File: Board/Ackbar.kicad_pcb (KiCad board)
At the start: 2 copper layers, 101.6 x 50.8 mm, 14 parts, among them J1 TOF, J2 GNSS, J3 HALL, J4 MOTOR, J5 PWR_IN, J6 EPD, U1 ESP32-S3 Pico, U2 VREG, U3 TMC2209, U4 SN74LVC1G04DCKR

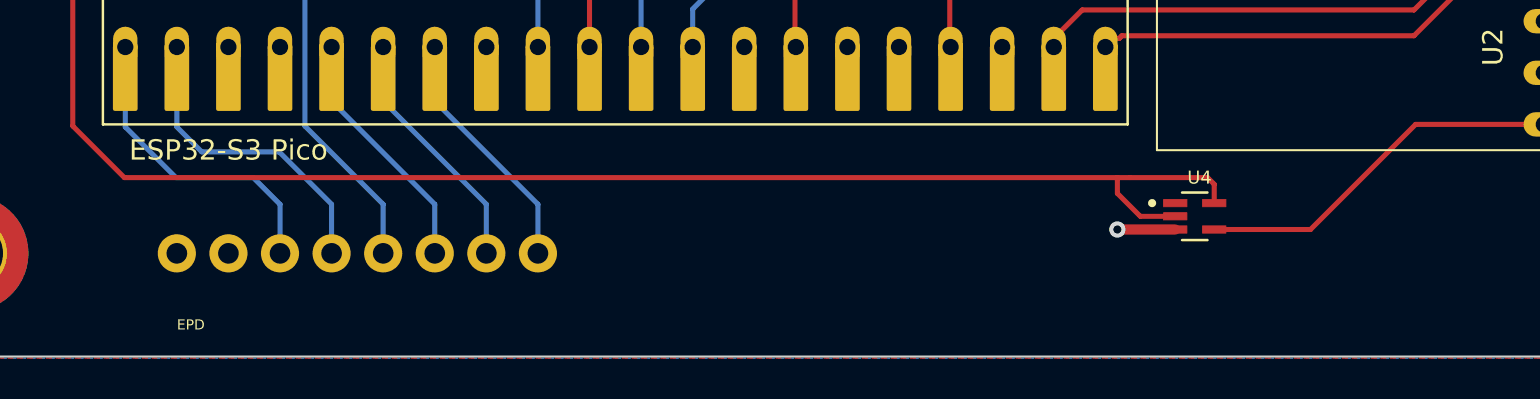
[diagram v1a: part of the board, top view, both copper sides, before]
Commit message: Larger footprint for inverter
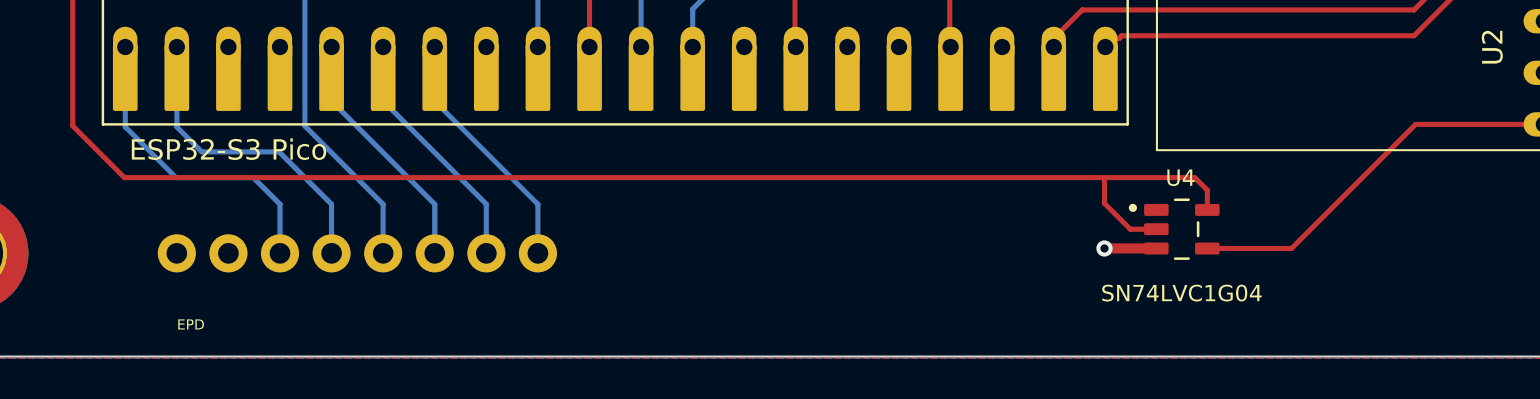
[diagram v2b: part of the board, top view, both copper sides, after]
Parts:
- U4: value SN74LVC1G04DCKR -> SN74LVC1G04; footprint Ackbar:SOT65P210X110-5N -> Ackbar:SOT95P280X145-5N
- moved U4 0.90 mm to (76.8, 56.5)
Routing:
- net Net-(U2-EN): track 18.4 -> 19.1 mm
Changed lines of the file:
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@@
       ))
   )
-  (footprint "Ackbar:SOT65P210X110-5N" (layer "F.Cu")
-    (at 77.47 55.88)
+  (footprint "Ackbar:SOT95P280X145-5N" (layer "F.Cu")
+    (at 76.835 56.515)
     (property "Check_prices" "https://www.snapeda.com/parts/SN74LVC1G04DCKR/Texas+Instruments/view-part/?ref=eda")
     (property "Description" "\nSingle 1.65-V to 5.5-V inverter\n")
@@
     (property "SnapEDA_Link" "https://www.snapeda.com/parts/SN74LVC1G04DCKR/Texas+Instruments/view-part/?ref=snap")
     (attr smd)
-    (fp_text reference "U4" (at 0.232 -1.9064) (layer "F.SilkS")
-        (effects (font (size 0.64 0.64) (thickness 0.15)))
-    )
-    (fp_text value "SN74LVC1G04DCKR" (at 4.7024 1.9064) (layer "F.Fab")
-        (effects (font (size 0.64 0.64) (thickness 0.15)))
-    )
-    (fp_line (start -0.625 -1.17) (end 0.625 -1.17)
+    (fp_text reference "U4" (at -0.06 -2.508) (layer "F.SilkS")
+        (effects (font (size 0.8 0.8) (thickness 0.15)))
+    )
+    (fp_text value "SN74LVC1G04" (at 0 3.175) (layer "F.SilkS")
+        (effects (font (size 0.8 0.8) (thickness 0.15)))
+    )
+    (fp_line (start -0.33 -1.45) (end 0.33 -1.45)
       (stroke (width 0.127) (type solid)) (layer "F.SilkS"))
-    (fp_line (start 0.625 1.17) (end -0.625 1.17)
+    (fp_line (start 0.33 1.45) (end -0.33 1.45)
       (stroke (width 0.127) (type solid)) (layer "F.SilkS"))
-    (fp_circle (center -2.1 -0.65) (end -2 -0.65)
+    (fp_line (start 0.8 -0.335) (end 0.8 0.335)
+      (stroke (width 0.127) (type solid)) (layer "F.SilkS"))
+    (fp_circle (center -2.41 -1.05) (end -2.31 -1.05)
       (stroke (width 0.2) (type solid)) (fill none) (layer "F.SilkS"))
-    (fp_line (start -1.81 -1.33) (end 1.81 -1.33)
+    (fp_line (start -2.11 -1.7) (end 2.11 -1.7)
       (stroke (width 0.05) (type solid)) (layer "F.CrtYd"))
-    (fp_line (start -1.81 1.33) (end -1.81 -1.33)
+    (fp_line (start -2.11 1.7) (end -2.11 -1.7)
       (stroke (width 0.05) (type solid)) (layer "F.CrtYd"))
-    (fp_line (start 1.81 -1.33) (end 1.81 1.33)
+    (fp_line (start 2.11 -1.7) (end 2.11 1.7)
       (stroke (width 0.05) (type solid)) (layer "F.CrtYd"))
-    (fp_line (start 1.81 1.33) (end -1.81 1.33)
+    (fp_line (start 2.11 1.7) (end -2.11 1.7)
       (stroke (width 0.05) (type solid)) (layer "F.CrtYd"))
-    (fp_line (start -0.625 -1) (end 0.625 -1)
+    (fp_line (start -0.8 -1.45) (end 0.8 -1.45)
       (stroke (width 0.127) (type solid)) (layer "F.Fab"))
-    (fp_line (start -0.625 1) (end -0.625 -1)
+    (fp_line (start -0.8 1.45) (end -0.8 -1.45)
       (stroke (width 0.127) (type solid)) (layer "F.Fab"))
-    (fp_line (start 0.625 -1) (end 0.625 1)
+    (fp_line (start 0.8 -1.45) (end 0.8 1.45)
       (stroke (width 0.127) (type solid)) (layer "F.Fab"))
-    (fp_line (start 0.625 1) (end -0.625 1)
+    (fp_line (start 0.8 1.45) (end -0.8 1.45)
       (stroke (width 0.127) (type solid)) (layer "F.Fab"))
-    (fp_circle (center -2.1 -0.65) (end -2 -0.65)
+    (fp_circle (center -2.41 -1.05) (end -2.31 -1.05)
       (stroke (width 0.2) (type solid)) (fill none) (layer "F.Fab"))
-    (pad "1" smd roundrect (at -0.96 -0.65) (size 1.19 0.4) (layers "F.Cu" "F.Paste" "F.Mask") (roundrect_rratio 0.05)
+    (pad "1" smd roundrect (at -1.255 -0.95) (size 1.21 0.59) (layers "F.Cu" "F.Paste" "F.Mask") (roundrect_rratio 0.15)
       (solder_mask_margin 0.102))
-    (pad "2" smd roundrect (at -0.96 0) (size 1.19 0.4) (layers "F.Cu" "F.Paste" "F.Mask") (roundrect_rratio 0.05)
+    (pad "2" smd roundrect (at -1.255 0) (size 1.21 0.59) (layers "F.Cu" "F.Paste" "F.Mask") (roundrect_rratio 0.15)
       (net 17 "Net-(U1-VBUS)") (pinfunction "A") (pintype "input") (solder_mask_margin 0.102))
-    (pad "3" smd roundrect (at -0.96 0.65) (size 1.19 0.4) (layers "F.Cu" "F.Paste" "F.Mask") (roundrect_rratio 0.05)
+    (pad "3" smd roundrect (at -1.255 0.95) (size 1.21 0.59) (layers "F.Cu" "F.Paste" "F.Mask") (roundrect_rratio 0.15)
       (net 9 "/GND") (pinfunction "GND") (pintype "power_in") (solder_mask_margin 0.102))
-    (pad "4" smd roundrect (at 0.96 0.65) (size 1.19 0.4) (layers "F.Cu" "F.Paste" "F.Mask") (roundrect_rratio 0.05)
+    (pad "4" smd roundrect (at 1.255 0.95) (size 1.21 0.59) (layers "F.Cu" "F.Paste" "F.Mask") (roundrect_rratio 0.15)
       (net 41 "Net-(U2-EN)") (pinfunction "Y") (pintype "output") (solder_mask_margin 0.102))
-    (pad "5" smd roundrect (at 0.96 -0.65) (size 1.19 0.4) (layers "F.Cu" "F.Paste" "F.Mask") (roundrect_rratio 0.05)
+    (pad "5" smd roundrect (at 1.255 -0.95) (size 1.21 0.59) (layers "F.Cu" "F.Paste" "F.Mask") (roundrect_rratio 0.15)
       (net 17 "Net-(U1-VBUS)") (pinfunction "VCC") (pintype "power_in") (solder_mask_margin 0.102))
   )
@@
     (effects (font (size 2.54 2.54) (thickness 0.15)) (justify left bottom))
   )
-  (segment (start 73.66 56.53) (end 76.51 56.53) (width 0.5) (layer "F.Cu") (net 9))
-  (via (at 73.66 56.53) (size 0.8) (drill 0.4) (layers "F.Cu" "B.Cu") (net 9))
+  (segment (start 73.025 57.465) (end 75.58 57.465) (width 0.5) (layer "F.Cu") (net 9))
+  (via (at 73.025 57.465) (size 0.8) (drill 0.4) (layers "F.Cu" "B.Cu") (net 9))
   (segment (start 99.06 31.115) (end 78.74 31.115) (width 0.5) (layer "F.Cu") (net 11))
   (segment (start 78.74 31.115) (end 76.878 29.253) (width 0.5) (layer "F.Cu") (net 11))
@@
   (segment (start 67.988 20.998) (end 67.988 17.064334) (width 0.25) (layer "B.Cu") (net 14))
   (segment (start 70.528 29.764334) (end 70.528 23.538) (width 0.25) (layer "B.Cu") (net 14))
-  (segment (start 78.43 54.3) (end 78.105 53.975) (width 0.25) (layer "F.Cu") (net 17))
+  (segment (start 72.39 53.975) (end 24.765 53.975) (width 0.25) (layer "F.Cu") (net 17))
+  (segment (start 73.025 55.245) (end 73.025 53.975) (width 0.25) (layer "F.Cu") (net 17))
+  (segment (start 24.765 53.975) (end 22.225 51.435) (width 0.25) (layer "F.Cu") (net 17))
+  (segment (start 22.225 32.347334) (end 24.808 29.764334) (width 0.25) (layer "F.Cu") (net 17))
+  (segment (start 78.105 54.61) (end 77.47 53.975) (width 0.25) (layer "F.Cu") (net 17))
+  (segment (start 78.09 54.625) (end 78.105 54.61) (width 0.25) (layer "F.Cu") (net 17))
+  (segment (start 75.58 56.515) (end 74.295 56.515) (width 0.25) (layer "F.Cu") (net 17))
+  (segment (start 78.09 55.565) (end 78.09 54.625) (width 0.25) (layer "F.Cu") (net 17))
+  (segment (start 74.295 56.515) (end 73.025 55.245) (width 0.25) (layer "F.Cu") (net 17))
   (segment (start 22.225 51.435) (end 22.225 32.347334) (width 0.25) (layer "F.Cu") (net 17))
-  (segment (start 22.225 32.347334) (end 24.808 29.764334) (width 0.25) (layer "F.Cu") (net 17))
-  (segment (start 78.43 55.23) (end 78.43 54.3) (width 0.25) (layer "F.Cu") (net 17))
-  (segment (start 73.66 54.751452) (end 74.788548 55.88) (width 0.25) (layer "F.Cu") (net 17))
-  (segment (start 24.765 53.975) (end 22.225 51.435) (width 0.25) (layer "F.Cu") (net 17))
-  (segment (start 74.295 53.975) (end 24.765 53.975) (width 0.25) (layer "F.Cu") (net 17))
-  (segment (start 73.66 53.975) (end 73.66 54.751452) (width 0.25) (layer "F.Cu") (net 17))
-  (segment (start 78.105 53.975) (end 74.295 53.975) (width 0.25) (layer "F.Cu") (net 17))
-  (segment (start 74.788548 55.88) (end 76.51 55.88) (width 0.25) (layer "F.Cu") (net 17))
+  (segment (start 77.47 53.975) (end 72.39 53.975) (width 0.25) (layer "F.Cu") (net 17))
   (segment (start 65.405 47.119334) (end 65.448 47.119334) (width 0.25) (layer "F.Cu") (net 18))
   (segment (start 65.405 41.275) (end 65.405 47.119334) (width 0.25) (layer "F.Cu") (net 18))
@@
   (segment (start 89.578 27.224334) (end 89.578 17.188) (width 0.5) (layer "F.Cu") (net 40))
   (segment (start 89.578 17.188) (end 89.535 17.145) (width 0.5) (layer "B.Cu") (net 40))
-  (segment (start 83.17 56.53) (end 88.345666 51.354334) (width 0.25) (layer "F.Cu") (net 41))
-  (segment (start 78.43 56.53) (end 83.17 56.53) (width 0.25) (layer "F.Cu") (net 41))
+  (segment (start 82.235 57.465) (end 88.345666 51.354334) (width 0.25) (layer "F.Cu") (net 41))
   (segment (start 88.345666 51.354334) (end 94.658 51.354334) (width 0.25) (layer "F.Cu") (net 41))
+  (segment (start 78.09 57.465) (end 82.235 57.465) (width 0.25) (layer "F.Cu") (net 41))
   (zone (net 10) (net_name "/3V3") (layer "F.Cu") (hatch edge 0.5)
     (priority 1)

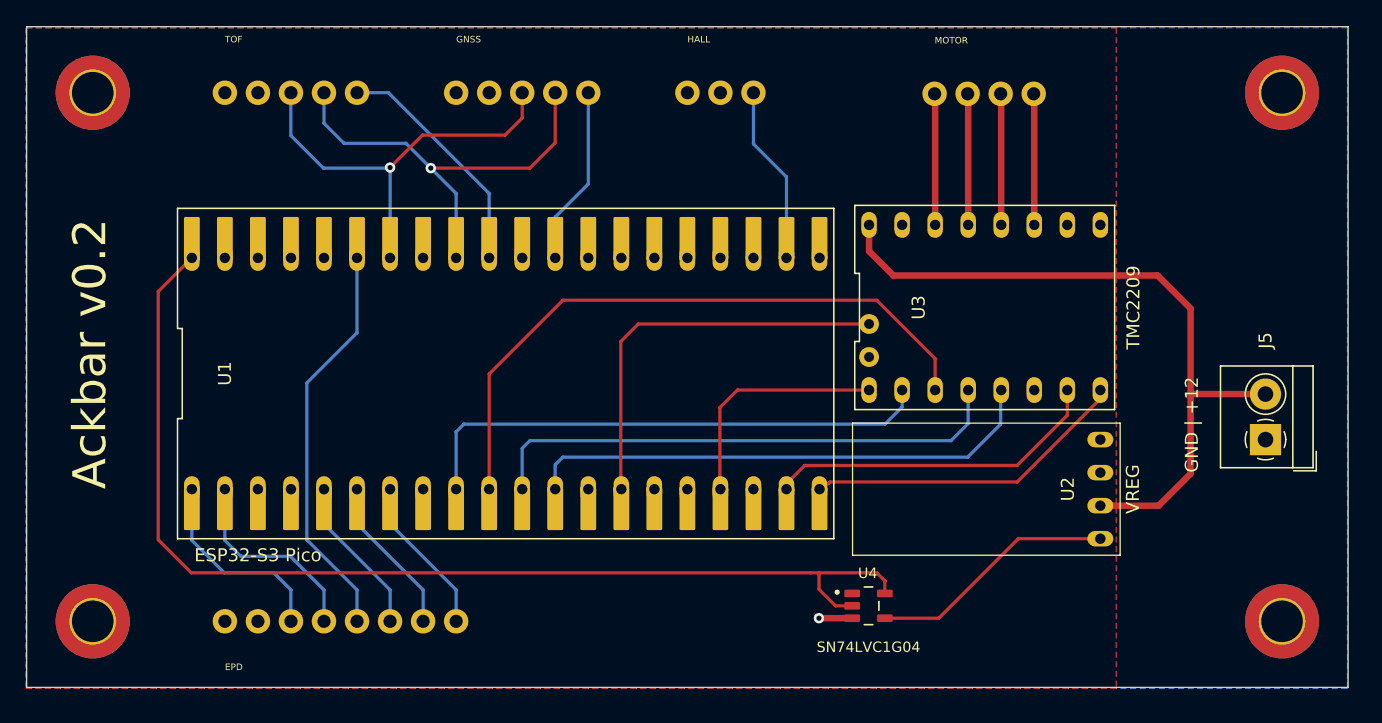
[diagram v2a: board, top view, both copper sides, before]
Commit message: cleanup vreg inhibit
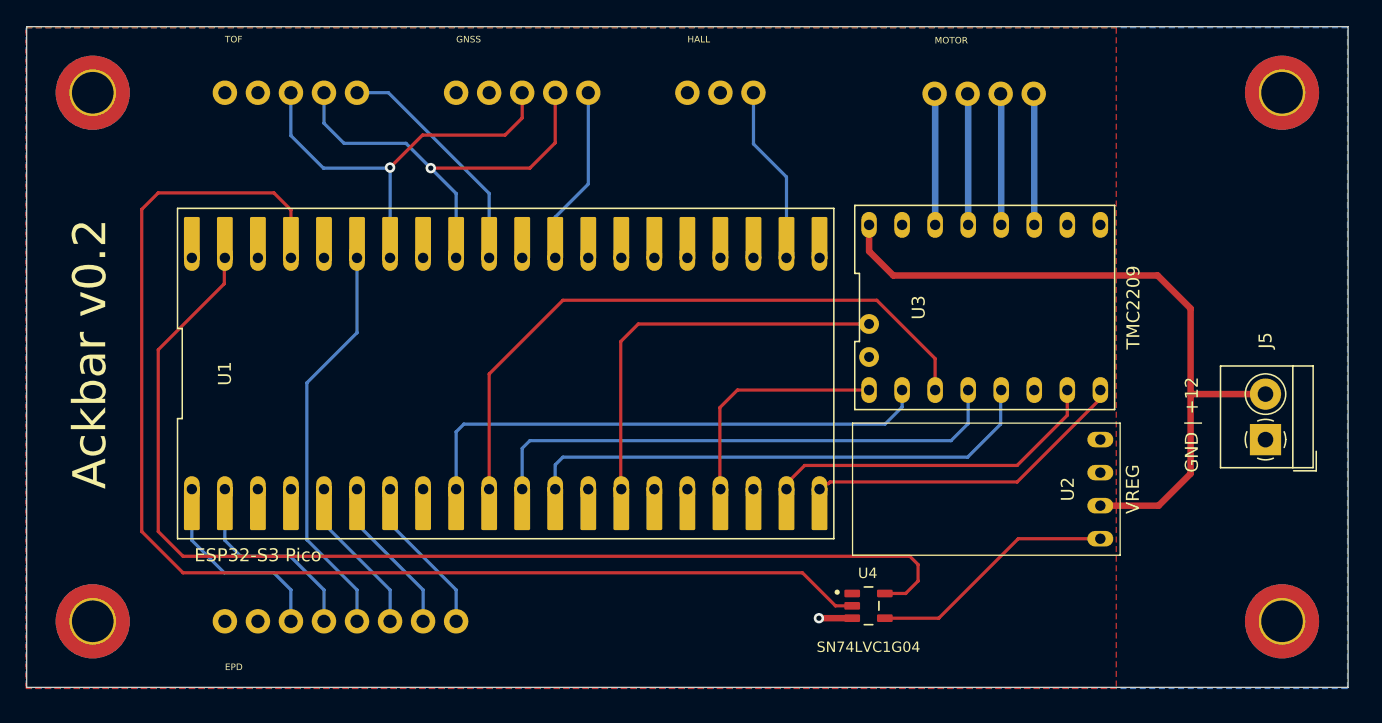
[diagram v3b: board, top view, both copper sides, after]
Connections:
- U1 pad 37: unconnected-(U1-3V3_EN-Pad37) -> Net-(U1-3V3_EN)
- U1 pad 39: unconnected-(U1-VSYS-Pad39) -> Net-(U1-VSYS)
- U1 pad 40: Net-(U1-VBUS) -> unconnected-(U1-VBUS-Pad40)
- U4 pad 2: Net-(U1-VBUS) -> Net-(U1-3V3_EN)
- U4 pad 5: Net-(U1-VBUS) -> Net-(U1-VSYS)
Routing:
- net Net-(U1-3V3_EN): track 0.00 -> 98.0 mm
- net Net-(U1-VSYS): track 0.00 -> 86.8 mm
- net Net-(U1-VBUS): track 85.2 -> 0.00 mm
- net /EPD_RST: track 12.3 -> 9.60 mm
- net /EPD_DC: track 12.3 -> 9.60 mm
- net /EPD_BUSY: track 12.3 -> 9.60 mm
- net /STP_DIR: track 25.0 -> 24.3 mm

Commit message: Re-route PCB and move USB C connector to board edge
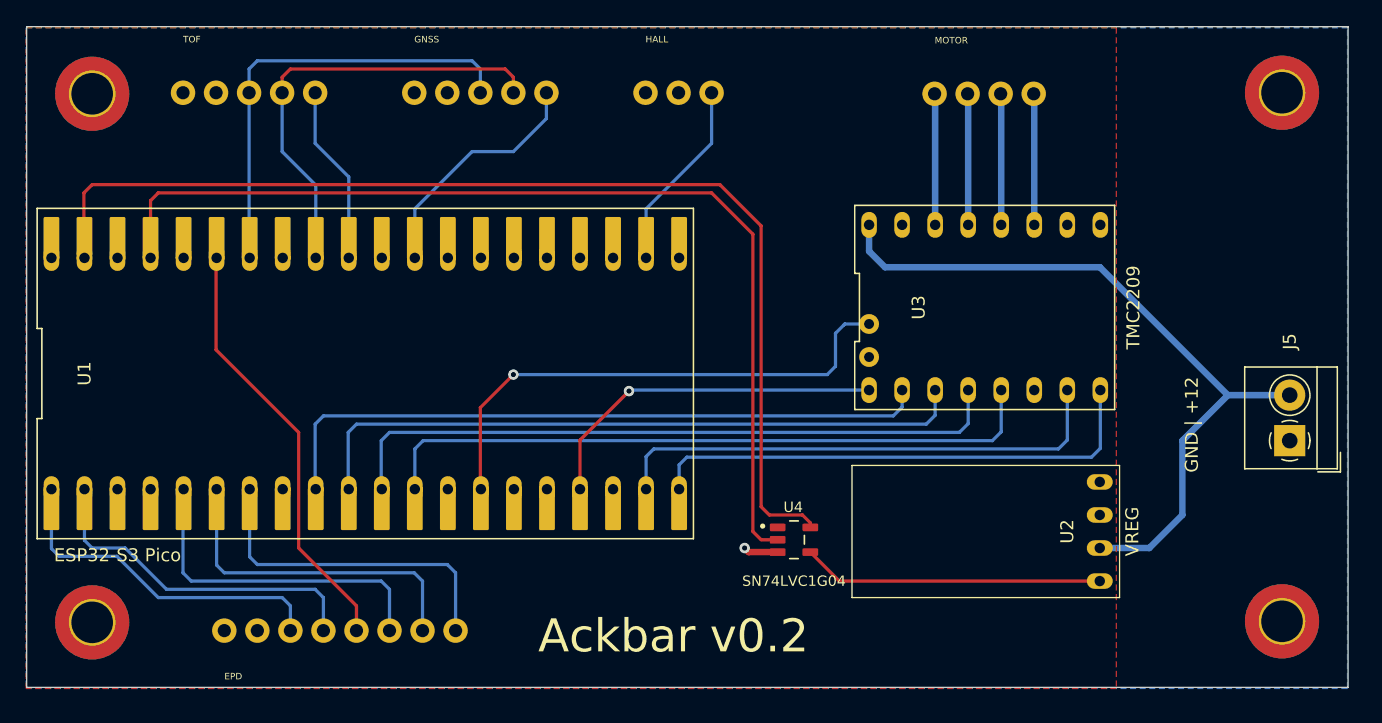
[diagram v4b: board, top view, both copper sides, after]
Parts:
- moved U1 10.8 mm to (38.1, 38.7)
- moved U4 7.66 mm to (71.1, 51.4)
- moved U2 3.26 mm to (94.6, 50.8)
- moved J2 3.22 mm to (41.9, 17.1)
- moved J3 3.22 mm to (59.7, 17.1)
- moved J1 3.22 mm to (24.1, 17.1)
- moved J5 1.86 mm to (109.2, 43.8)
- moved J6 0.72 mm to (27.3, 58.4)
- moved REF** 0.09 mm to (17.1, 17.1)
- moved REF** 0.09 mm to (17.1, 57.8)
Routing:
- net Net-(U1-3V3_EN): track 98.0 -> 77.3 mm
- net /EPD_RST: track 9.60 -> 26.0 mm
- net /EPD_BUSY: track 9.60 -> 26.0 mm
- net /EPD_DC: track 9.60 -> 26.0 mm
- net /STP_DIR: track 24.3 -> 39.3 mm
- net /STP_STEP: track 25.7 -> 39.3 mm
- net /STP_PDN: track 40.0 -> 51.9 mm
- net /STP_MS3: track 40.8 -> 51.9 mm
- net /STP_MS1: track 40.8 -> 51.9 mm
- net /MOSI: track 15.5 -> 26.7 mm
- net /SCK: track 15.5 -> 26.7 mm
- net /STP_EN: track 17.9 -> 27.6 mm, vias 0 -> 1
- net /STP_DIAG: track 30.6 -> 40.3 mm, vias 0 -> 1
- net /GNSS_INT: track 13.8 -> 18.8 mm
- net /TOF_XSHUT: track 18.3 -> 13.8 mm
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
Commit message: WIP of firmware refactoring
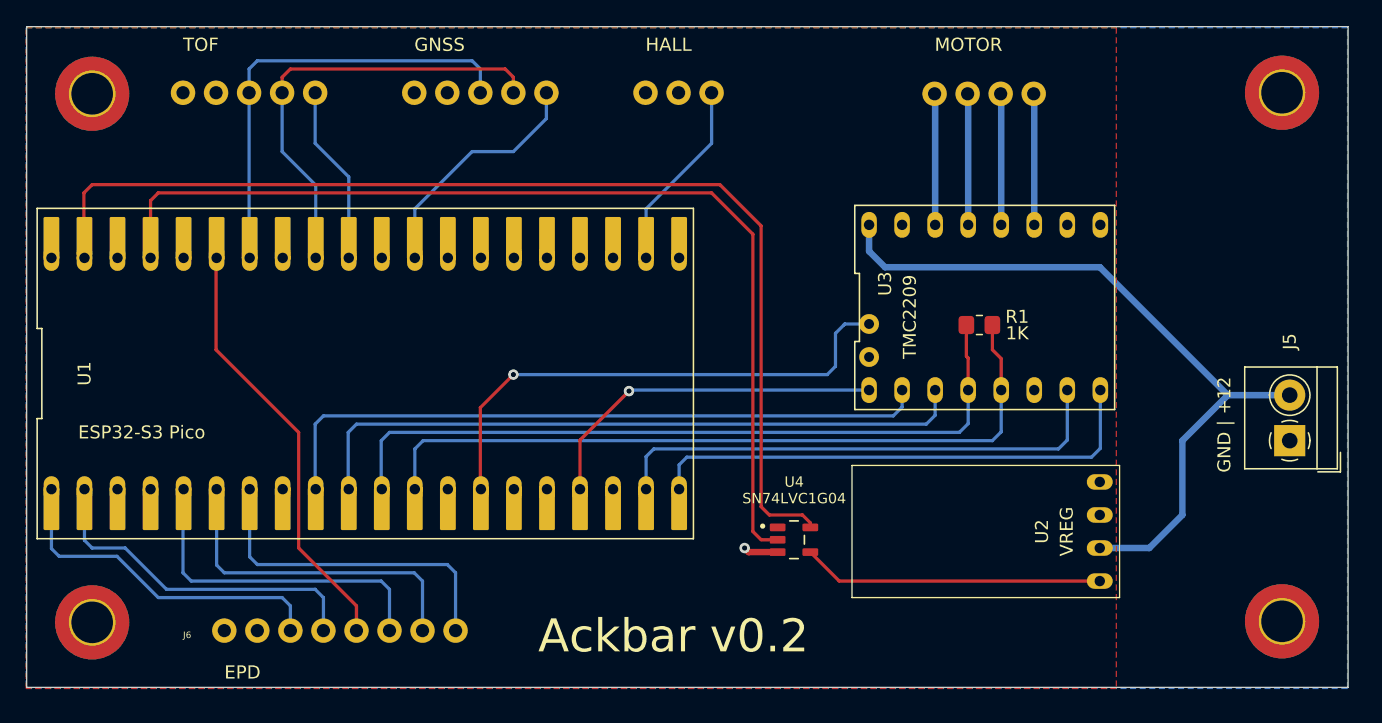
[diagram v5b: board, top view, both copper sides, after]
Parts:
- added R1: 1K, Resistor_SMD:R_0805_2012Metric_Pad1.20x1.40mm_HandSolder, F.Cu at (85.4, 34.9)
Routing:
- net /STP_PDN: track 51.9 -> 57.2 mm
- net /STP_MS3: track 51.9 -> 57.0 mm
